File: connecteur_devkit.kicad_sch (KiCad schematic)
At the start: 8 parts, among them J10 OLED_SPI_2x8, J5 DEVKIT_C2000_ROW_A, J6 DEVKIT_C2000_ROW_B, J7 ESP32_C6_DEVKITC_1_J1, J8 ESP32_C6_DEVKITC_1_J3, U4 ER-OLEDM032-1

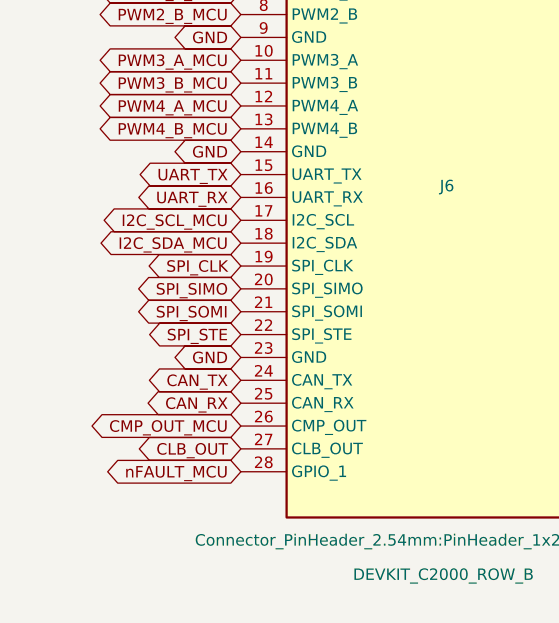
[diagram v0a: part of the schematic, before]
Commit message: Corrige ADC-2 (I_SHUNT1_CMP/I_SHUNT2_CMP) et protege 11 signaux nappe (decisions #18-19)
ADC-2 ne cablait que la voie filtree (I_shunt1/I_shunt2) et oubliait le
chemin direct comparateur que la decision #4 impose. Ajoute en
consommant 2 des 6 reserves, sans adjacence avec la voie filtree (les
deux chemins doivent rester independants).

11 signaux cables en decision #17 n'avaient aucune protection
(CLB_OUT, UART_TX/RX, SPI_CLK/SIMO/SOMI/STE, CAN_TX/RX, et les deux
I_SHUNT*_CMP une fois ajoutes) alors que les 23 autres signaux du
connecteur devkit en ont une. Nouvelle feuille protection_nappe.kicad_sch,
11 trios copies depuis un trio reel (protection_devkit3.kicad_sch) plutot
que redessines - BAT54S + R + 100pF, R=100R standard sauf les deux
I_SHUNT*_CMP a 22R (decision #4 : Rs<=50 Ohm sur ce chemin, 100R le
depasserait).

9 labels renommes en _MCU cote connecteur_devkit.kicad_sch (meme
convention que les 23 trios existants : le nom brut cote nappe, le nom
_MCU cote connecteur devkit, jamais l'inverse).

Egalement loggee : decision #18, le decoupage 100nF des 6 nappes pose
manuellement par l'utilisateur dans une session precedente.

Verifie par kicad-cli sch erc, compare par type de violation : les 11
isolated_pin_label vises ont disparu, aucune autre categorie n'augmente
sauf endpoint_off_grid (+33, un par composant neuf, meme defaut
pre-existant que les 23 trios deja en place).
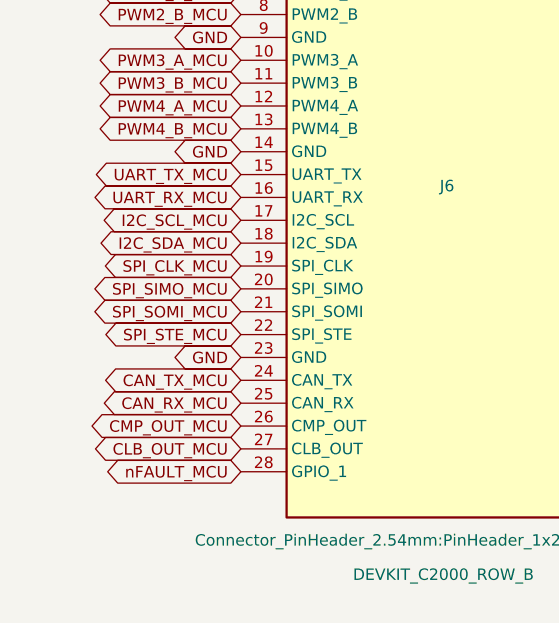
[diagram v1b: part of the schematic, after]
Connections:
- net CAN_RX renamed CAN_RX_MCU
- net CAN_TX renamed CAN_TX_MCU
- net CLB_OUT renamed CLB_OUT_MCU
- net SPI_CLK renamed SPI_CLK_MCU
- net SPI_SIMO renamed SPI_SIMO_MCU
- net SPI_SOMI renamed SPI_SOMI_MCU
- net SPI_STE renamed SPI_STE_MCU
- net UART_RX renamed UART_RX_MCU
- net UART_TX renamed UART_TX_MCU
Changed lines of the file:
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@@
 		)
 	)
-	(global_label "UART_TX"
+	(global_label "UART_TX_MCU"
 		(shape bidirectional)
 		(at 45.974 152.4 180)
@@
 		)
 	)
-	(global_label "SPI_SOMI"
+	(global_label "SPI_SOMI_MCU"
 		(shape bidirectional)
 		(at 45.974 167.64 180)
@@
 		)
 	)
-	(global_label "SPI_CLK"
+	(global_label "SPI_CLK_MCU"
 		(shape bidirectional)
 		(at 45.974 162.56 180)
@@
 		)
 	)
-	(global_label "CAN_RX"
+	(global_label "CAN_RX_MCU"
 		(shape bidirectional)
 		(at 45.974 177.8 180)
@@
 		)
 	)
-	(global_label "CLB_OUT"
+	(global_label "CLB_OUT_MCU"
 		(shape bidirectional)
 		(at 45.974 182.88 180)
@@
 		)
 	)
-	(global_label "CAN_TX"
+	(global_label "CAN_TX_MCU"
 		(shape bidirectional)
 		(at 45.974 175.26 180)
@@
 		)
 	)
-	(global_label "SPI_STE"
+	(global_label "SPI_STE_MCU"
 		(shape bidirectional)
 		(at 45.974 170.18 180)
@@
 		)
 	)
-	(global_label "UART_RX"
+	(global_label "UART_RX_MCU"
 		(shape bidirectional)
 		(at 45.974 154.94 180)
@@
 		)
 	)
-	(global_label "SPI_SIMO"
+	(global_label "SPI_SIMO_MCU"
 		(shape bidirectional)
 		(at 45.974 165.1 180)

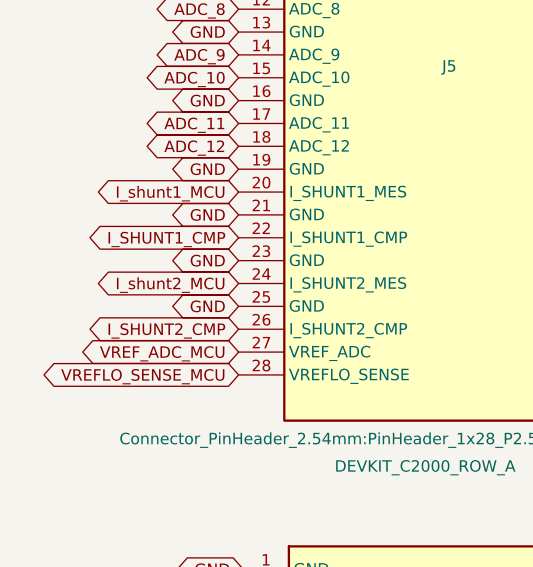
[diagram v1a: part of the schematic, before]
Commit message: Corrige le court-circuit du trio I_SHUNT1_CMP/I_SHUNT2_CMP (devkit)
Le connecteur devkit portait encore les labels bruts I_SHUNT1_CMP/
I_SHUNT2_CMP au lieu de la forme _MCU (oubli lors de la decision #19,
qui pretendait le contraire). Un global_label KiCad fusionnant par nom,
cela court-circuitait silencieusement le trio BAT54S/R/C deja pose : le
nom brut cote nappe et le nom (censement protege) cote MCU pointaient
vers le meme noeud. Invisible a l'ERC (fusion de deux labels valides,
pas une erreur de connectivite). Corrige en renommant les deux labels
devkit en I_SHUNT1_CMP_MCU/I_SHUNT2_CMP_MCU.

Necessite un nouveau "Update PCB from Schematic" : la synchronisation
precedente a eu lieu pendant que le bug etait encore present.
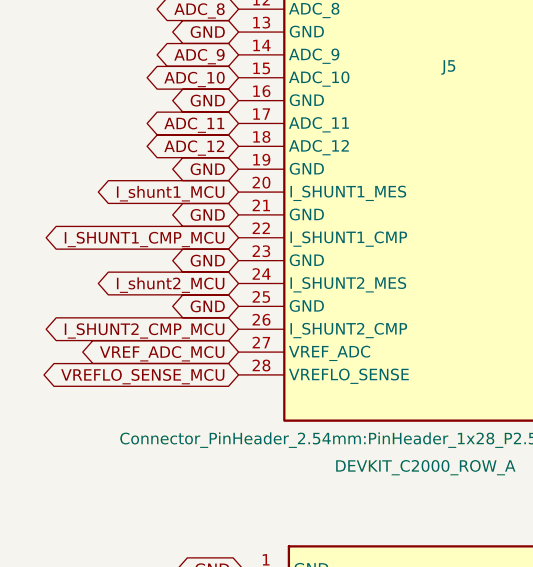
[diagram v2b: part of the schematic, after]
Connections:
- net I_SHUNT1_CMP renamed I_SHUNT1_CMP_MCU
- net I_SHUNT2_CMP renamed I_SHUNT2_CMP_MCU
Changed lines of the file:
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@@
 		)
 	)
-	(global_label "I_SHUNT2_CMP"
+	(global_label "I_SHUNT2_CMP_MCU"
 		(shape bidirectional)
 		(at 45.466 90.17 180)
@@
 		)
 	)
-	(global_label "I_SHUNT1_CMP"
+	(global_label "I_SHUNT1_CMP_MCU"
 		(shape bidirectional)
 		(at 45.466 80.01 180)

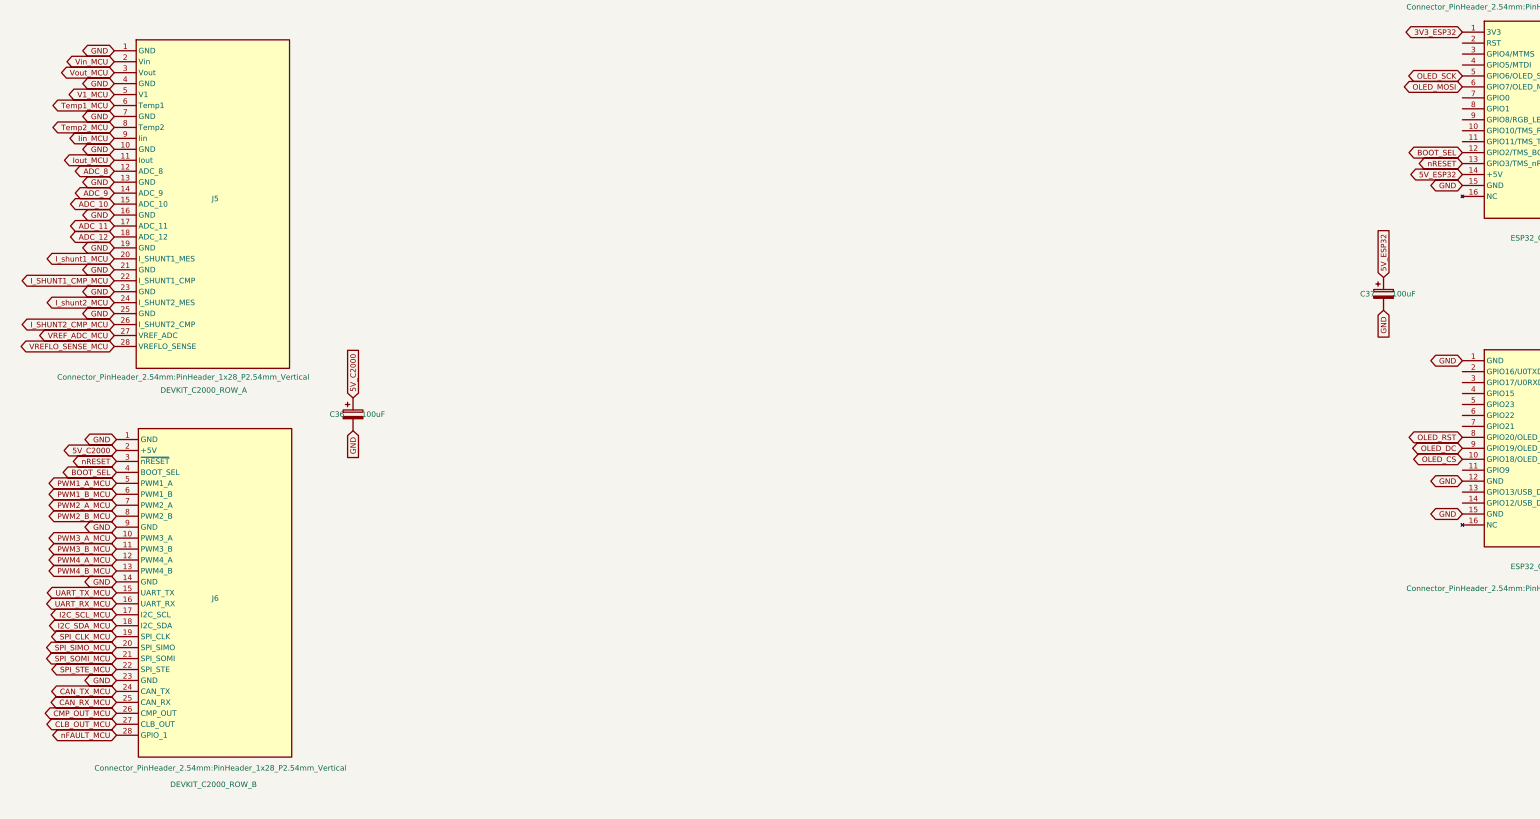
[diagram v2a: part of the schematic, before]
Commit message: CLB du F28P551 en mini-CPLD : report devkit, 4 trios, nappe logic (decision #20)
- Report sur connecteur_devkit.kicad_sch (symboles + labels reels, lib
  externe incluse) du reseequencement devkit (Iin/Iout/V1/Temp1/Temp2/
  ADC_8-12/I_SHUNT*_CMP/I_SHUNT*_MES deplaces) et des 4 broches neuves
  (Stage1_EN=GPIO9, Stage2_EN=GPIO20, HV_EN=GPIO21, Discharge=GPIO41).
- Corrige un erratum trouve en verifiant : protection_devkit3.kicad_sch
  gardait l'ancien nom nFAULT_MCU apres le renommage du connecteur en
  ~{FAULT_MCU}, coupant silencieusement le trio existant (meme categorie
  de bug que l'erratum ADC-2 de la decision #19).
- 4 nouveaux trios de protection D36-39/R35-38/C55-58, R=10R (signaux
  classes Rapide, decision explicite), pour les 4 sorties neuves.
- Nappe GPIO-2 renommee nappe "logic" (NAPPE_LOGIC, J13) : 9 reserves
  deviennent CLB_Out_1-4/CLB_In_1-5 (noms cosmetiques sur le connecteur
  uniquement, le net electrique reste le vrai nom de signal). 4 sorties
  protegees + 5 entrees tapees sans sacrifice (CAN_RX/CAN_TX, PWM2_B/
  PWM3_B/PWM4_B - deja protegees ailleurs, lues en plus ici).
- netclass_patterns, used_designators, doc/decisions.md #20,
  doc/nappes-shield.md, doc/brochage-devkit.csv mis a jour.

ERC : isolated_pin_label 9->5 (reste les 5 reserves ADC libres, hors
perimetre), pin_not_connected -9 (nappe logic cablee), aucune nouvelle
categorie.
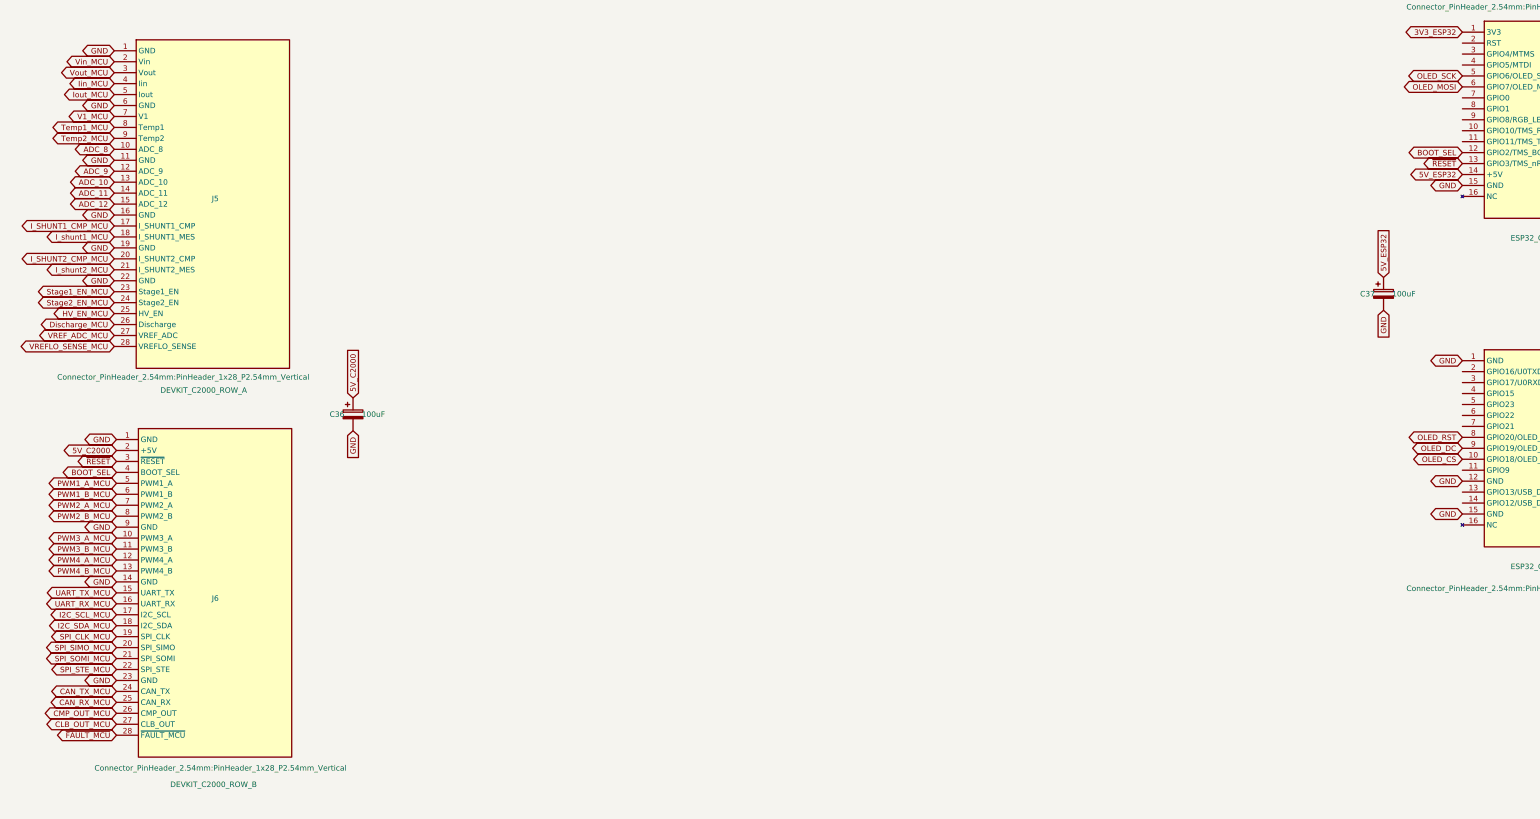
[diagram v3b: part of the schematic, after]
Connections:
- net ADC_10: now also J5.13 (ADC_10); no longer J5.15 (ADC_10)
- net ADC_11: now also J5.14 (ADC_11); no longer J5.17 (ADC_11)
- net ADC_12: now also J5.15 (ADC_12); no longer J5.18 (ADC_12)
- net ADC_8: now also J5.10 (ADC_8); no longer J5.12 (ADC_8)
- net ADC_9: now also J5.12 (ADC_9); no longer J5.14 (ADC_9)
- net GND: now also J5.11 (GND), J5.22 (GND), J5.6 (GND); no longer J5.10 (GND), J5.13 (GND), J5.21 (GND), J5.23 (GND), J5.25 (GND), J5.4 (GND), J5.7 (GND)
- net I_SHUNT1_CMP_MCU: now also J5.17 (I_SHUNT1_CMP); no longer J5.22 (I_SHUNT1_CMP)
- net I_SHUNT2_CMP_MCU: now also J5.20 (I_SHUNT2_CMP); no longer J5.26 (I_SHUNT2_CMP)
- net I_shunt1_MCU: now also J5.18 (I_SHUNT1_MES); no longer J5.20 (I_SHUNT1_MES)
- net I_shunt2_MCU: now also J5.21 (I_SHUNT2_MES); no longer J5.24 (I_SHUNT2_MES)
- net Iin_MCU: now also J5.4 (Iin); no longer J5.9 (Iin)
- net Iout_MCU: now also J5.5 (Iout); no longer J5.11 (Iout)
- net Temp1_MCU: now also J5.8 (Temp1); no longer J5.6 (Temp1)
- net Temp2_MCU: now also J5.9 (Temp2); no longer J5.8 (Temp2)
- net V1_MCU: now also J5.7 (V1); no longer J5.5 (V1)
- net nFAULT_MCU renamed ~{FAULT_MCU}
- net nRESET renamed ~{RESET}
- new net Discharge_MCU: J5.26 (Discharge)
- new net HV_EN_MCU: J5.25 (HV_EN)
- new net Stage1_EN_MCU: J5.23 (Stage1_EN)
- new net Stage2_EN_MCU: J5.24 (Stage2_EN)
